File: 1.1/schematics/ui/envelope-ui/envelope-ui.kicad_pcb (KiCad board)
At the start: 2 copper layers, 120 x 100 mm, 21 parts, among them U1 SW_SPST_Push_LED

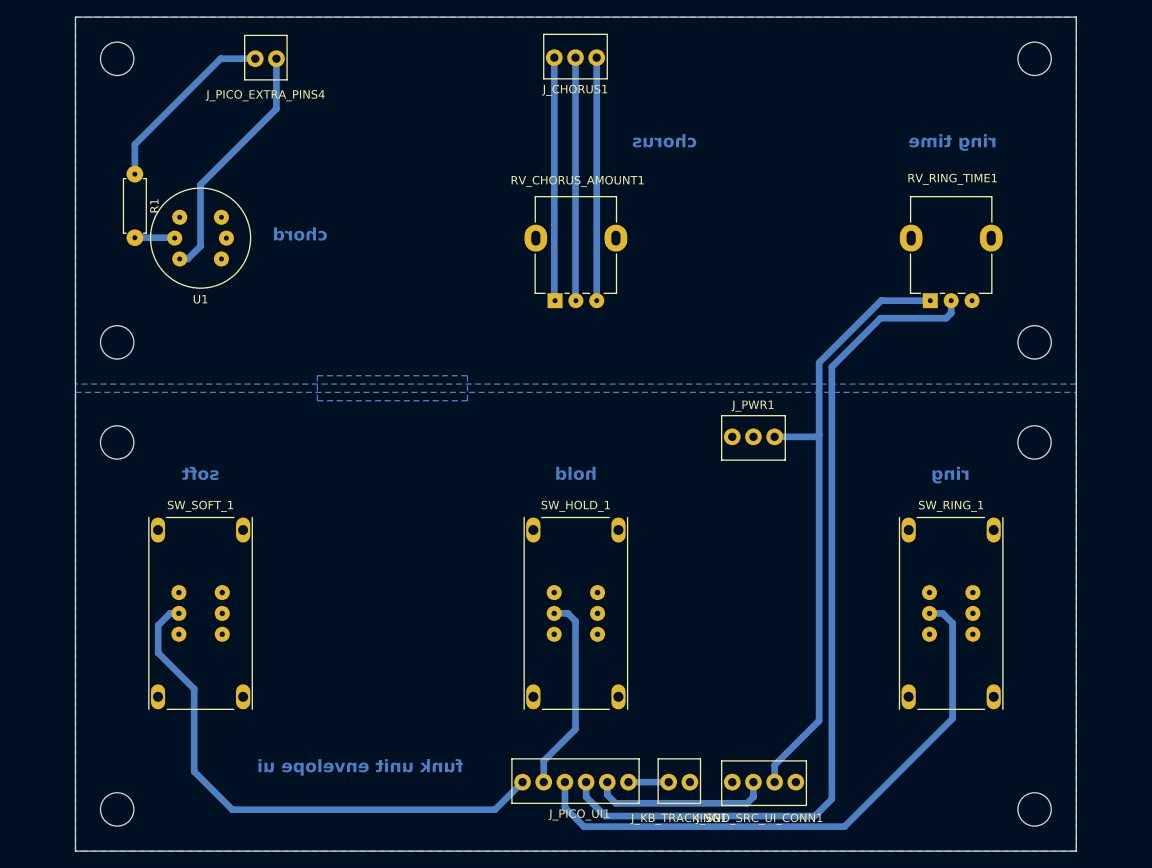
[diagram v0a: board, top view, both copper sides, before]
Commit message: Made envelope UI narrower
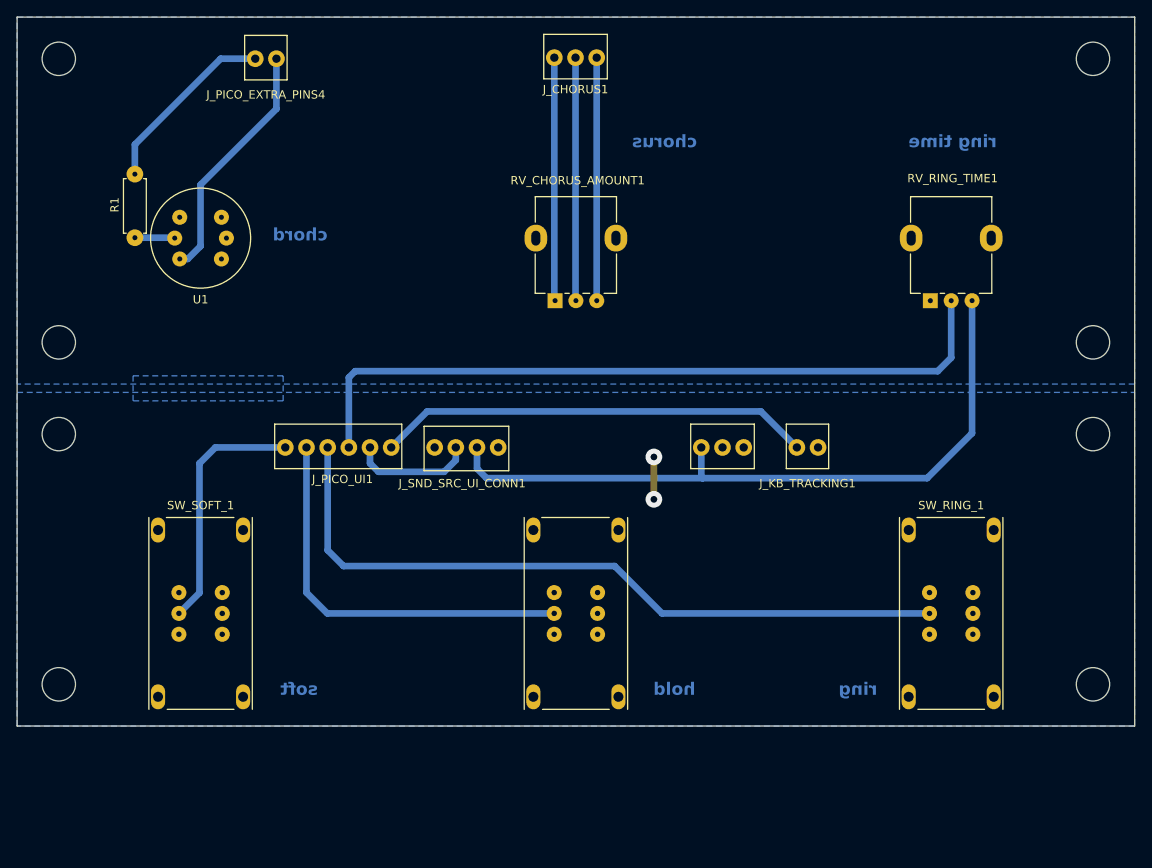
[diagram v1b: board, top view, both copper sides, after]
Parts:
- moved J_SND_SRC_UI_CONN1 53.7 mm to (130.7, 85.6)
- moved J_PICO_UI1 49.2 mm to (105.2, 85.6)
- moved J_KB_TRACKING1 43.0 mm to (166.5, 85.6)
- moved H3 16.6 mm to (202.0, 114.0)
- moved H4 16.6 mm to (78.0, 114.0)
- moved J_PWR1 8.88 mm to (155.0, 85.6), turned to 0 degrees
- moved H8 7.08 mm to (202.0, 84.0)
- moved H7 7.07 mm to (78.0, 84.0)
- moved H1 7.00 mm to (78.0, 39.0)
- moved H2 7.00 mm to (202.0, 39.0)
- moved H6 7.00 mm to (78.0, 73.0)
- moved H5 7.00 mm to (202.0, 73.0)
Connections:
- RV_RING_TIME1 pad 1: +3.3V -> GND
- RV_RING_TIME1 pad 3: GND -> +3.3V
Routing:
- net KB_TRACKING: track 4.83 -> 52.2 mm
- net SOFT: track 65.0 -> 30.1 mm
- net HOLD: track 23.8 -> 48.1 mm
- net RING: track 70.5 -> 87.6 mm
- net RING_TIME: track 103.3 -> 88.4 mm
- net +3.3V: track 74.4 -> 84.2 mm
- net GLIDE: track 21.6 -> 14.7 mm
- net GND: track 0.00 -> 5.08 mm, vias 0 -> 2
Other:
- board size 120 x 100 mm -> 134 x 85 mm
- board text removed: "funk unit envelope ui"
